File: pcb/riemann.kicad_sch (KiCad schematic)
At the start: 7 parts, among them SW61 Reset, U1 RaspberryPi_Pico

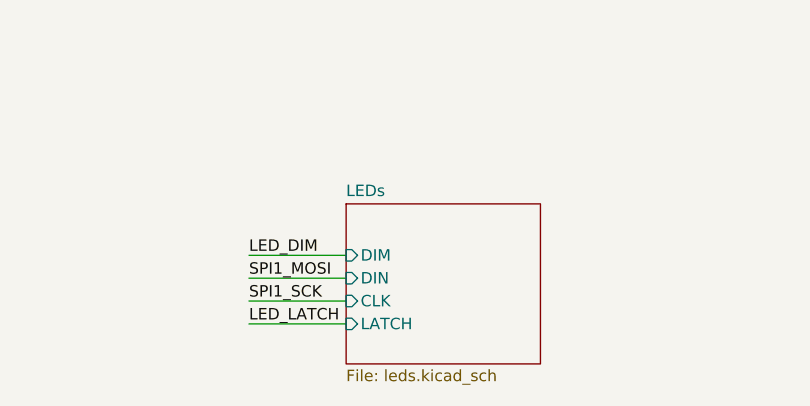
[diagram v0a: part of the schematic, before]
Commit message: Increase polling frequency of NKRO report
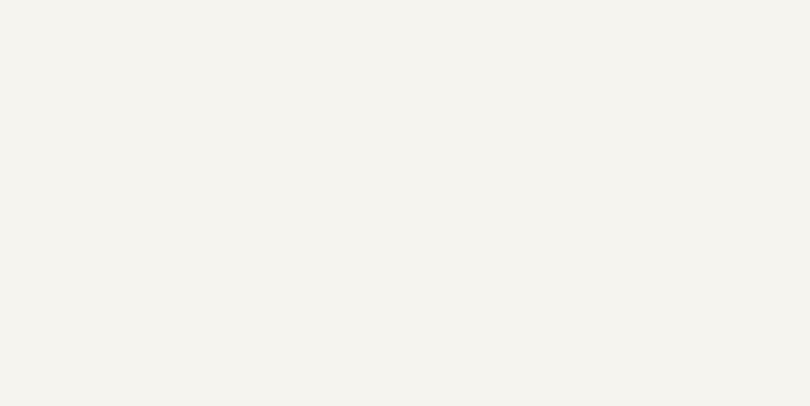
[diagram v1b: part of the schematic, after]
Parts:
- R12: footprint agausmann:R_Hybrid_SMD_THT -> Resistor_THT:R_Axial_DIN0204_L3.6mm_D1.6mm_P7.62mm_Horizontal
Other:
- removed sheet LEDs
